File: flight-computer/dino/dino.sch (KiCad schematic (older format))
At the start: 5 parts

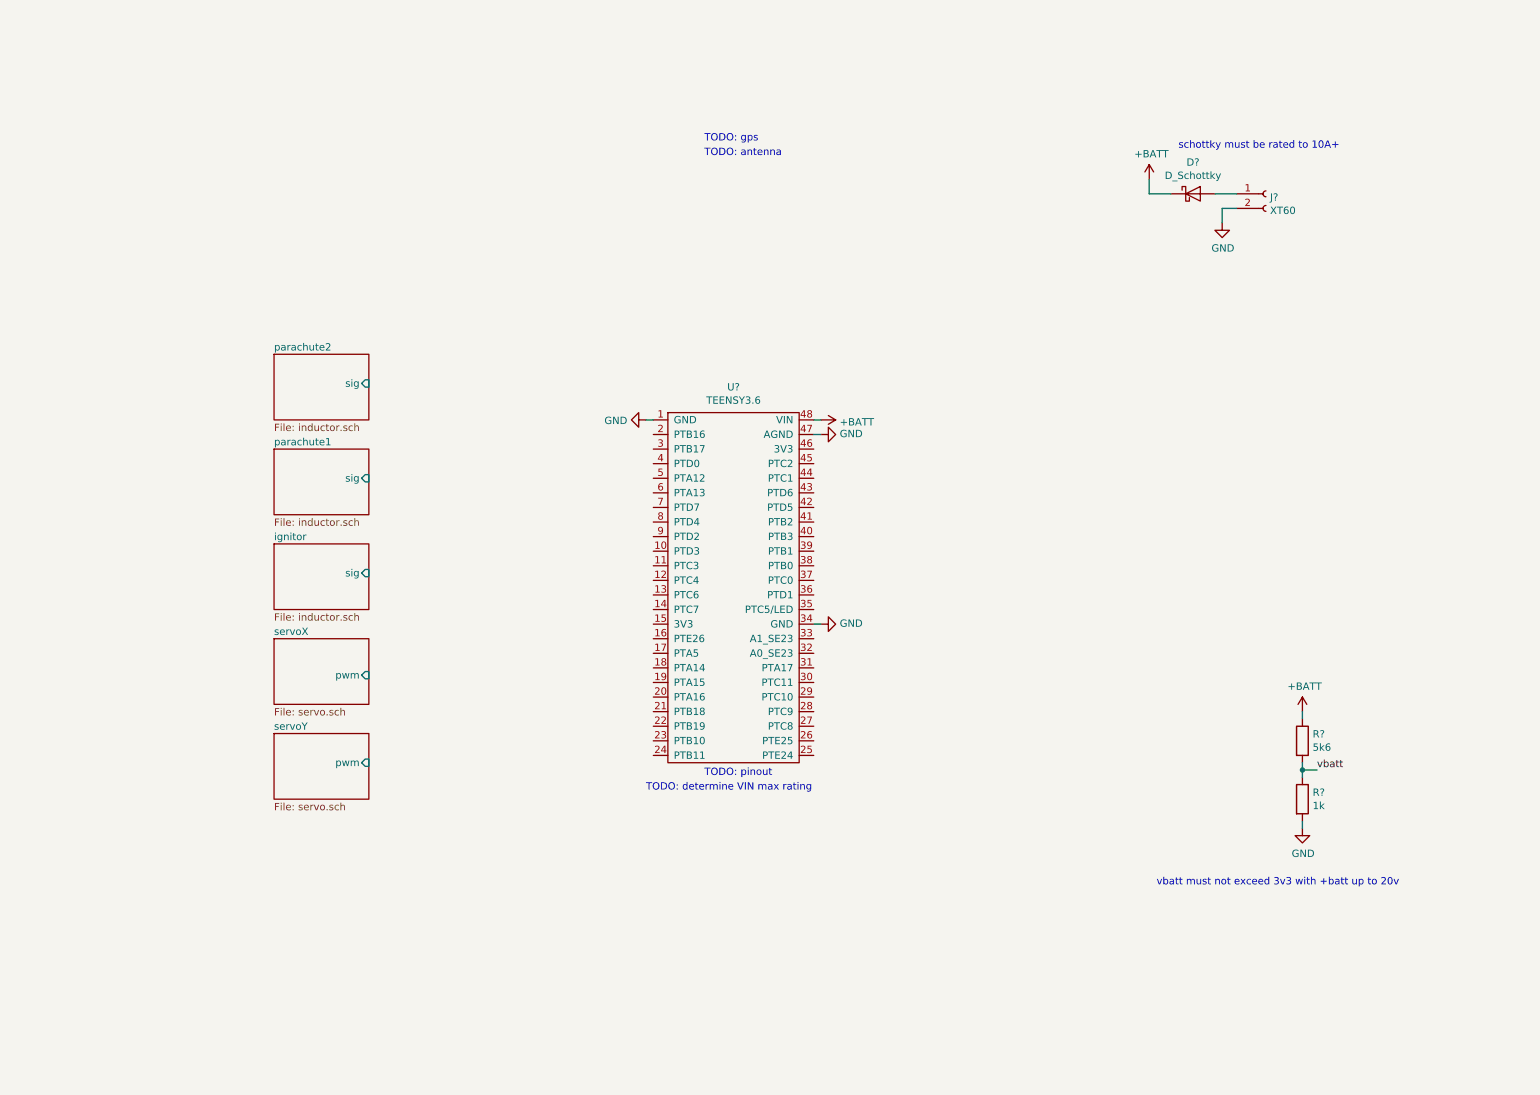
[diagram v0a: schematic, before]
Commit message: more pcb component selection
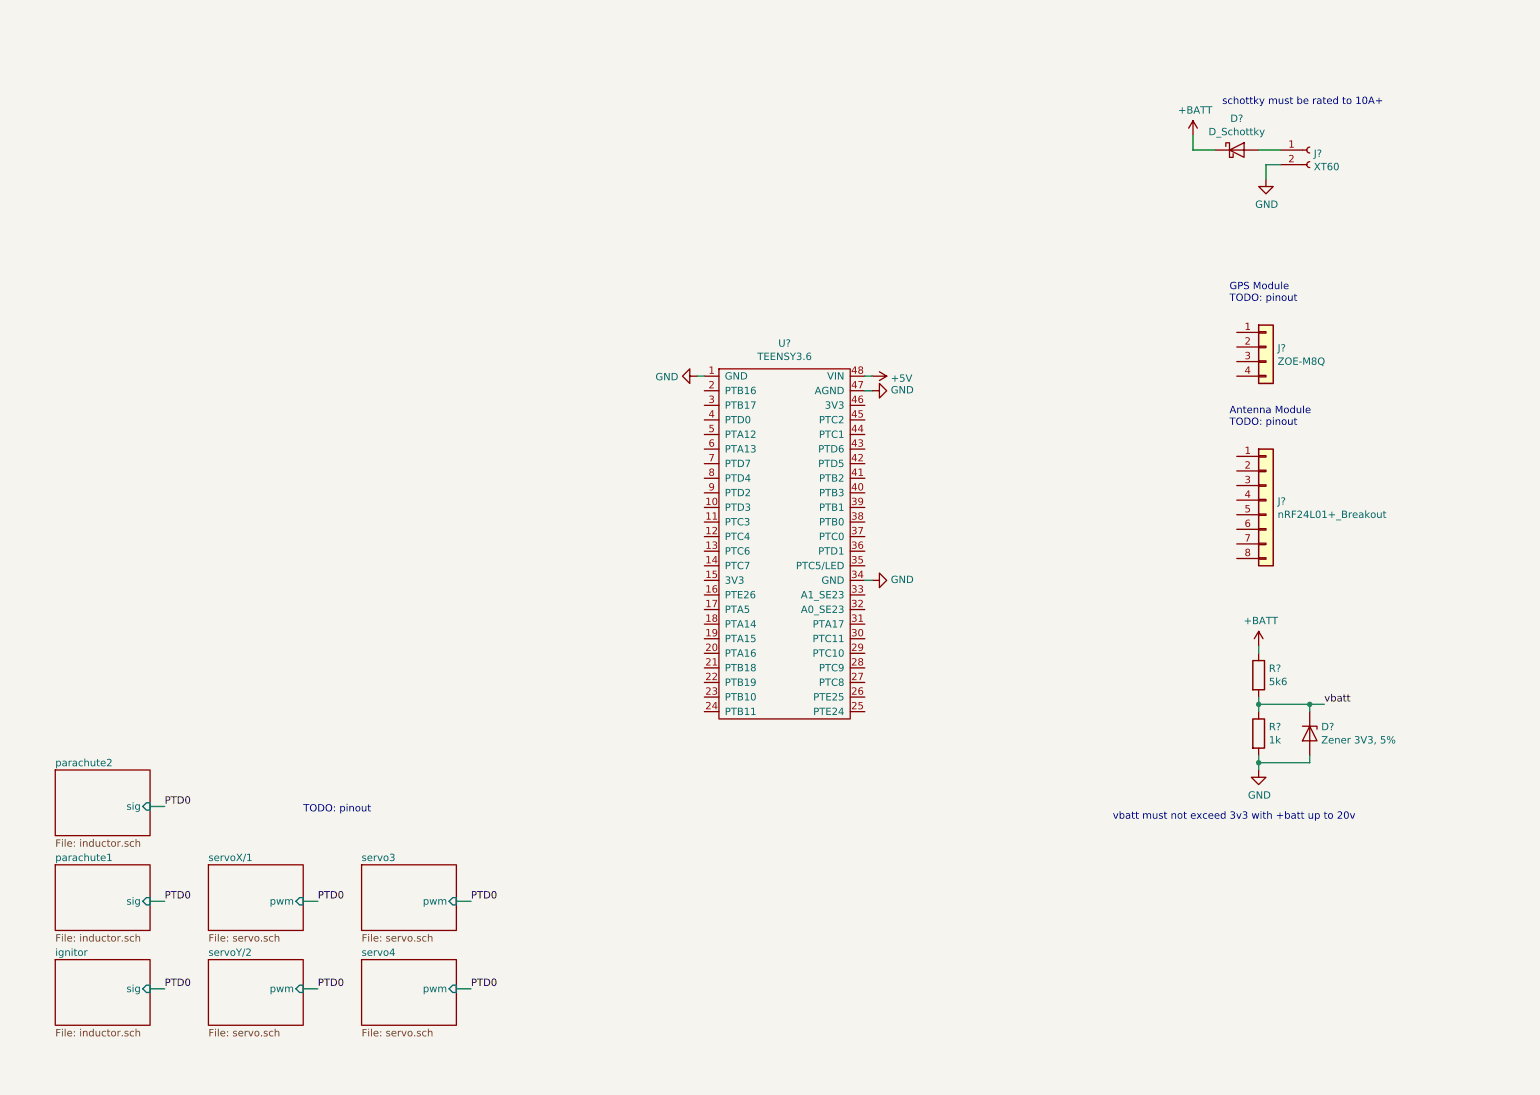
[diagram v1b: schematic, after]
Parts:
- added D?: Zener 3V3, 5%, symbol Device:D_Zener
- added J?: nRF24L01+_Breakout, symbol Connector_Generic:Conn_01x08
- added J?: ZOE-M8Q, symbol Connector_Generic:Conn_01x04
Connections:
- net +BATT: no longer U?.48 (VIN)
- net GND: now also D?.2 (A)
- net vbatt: now also D?.1 (K)
- new net +5V: U?.48 (VIN)
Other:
- note added: "Antenna Module\nTODO: pinout"
- note added: "GPS Module\nTODO: pinout"
- note removed: "TODO: antenna"
- note removed: "TODO: determine VIN max rating"
- note removed: "TODO: gps"
- moved on the sheet: D?, J?, R?, U?

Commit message: fc schematic fleshing-out and mcu docs
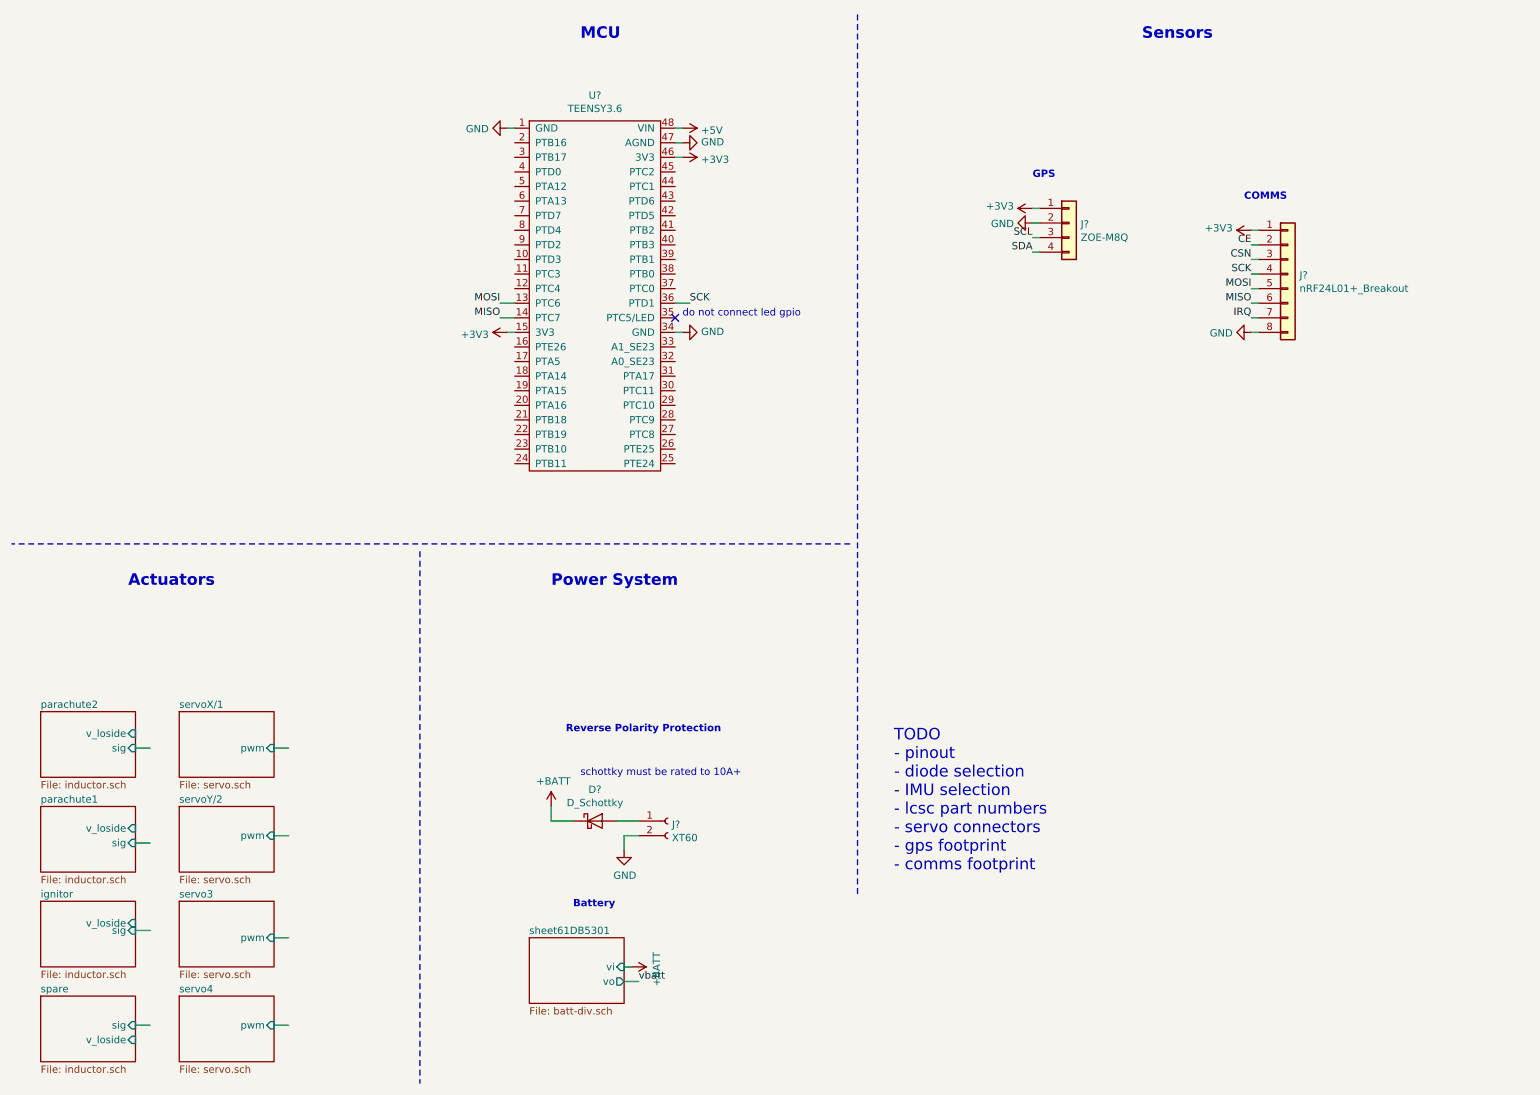
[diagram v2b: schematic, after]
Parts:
- removed D?: Zener 3V3, 5%, symbol Device:D_Zener
- removed R?: 5k6, symbol Device:R
- removed R?: 1k, symbol Device:R
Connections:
- net labels added: +3V3, CE, CSN, IRQ, MISO, MOSI, SCK, SCL, SDA
- net labels removed: PTD0
- wire segments 26 -> 36
- no-connect marks 0 -> 1
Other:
- note added: "Actuators"
- note added: "Battery"
- note added: "COMMS"
- note added: "GPS"
- note added: "MCU"
- note added: "Power System"
- note added: "Reverse Polarity Protection"
- note added: "Sensors"
- note added: "TODO\n- pinout\n- diode selection\n- IMU selection\n- lcsc part numbers\n- servo connectors\n- gps footprint\n- comms footprint"
- note added: "do not connect led gpio"
- note removed: "Antenna Module\nTODO: pinout"
- note removed: "GPS Module\nTODO: pinout"
- note removed: "TODO: pinout"
- note removed: "vbatt must not exceed 3v3 with +batt up to 20v"
- moved on the sheet: D?, J?, U?

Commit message: fc pinout and component selection. general cleanup
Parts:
- removed D?: D_Schottky, symbol Device:D_Schottky
- added C? (x3): 10u, Capacitor_Tantalum_SMD:CP_EIA-3216-18_Kemet-A, symbol Device:CP1_Small
- added D?: 40V 5A 550mV, Diode_SMD:D_SMA, symbol Device:D_Schottky
- added D? (x5): R, Diode_SMD:D_0603_1608Metric, symbol Device:LED_Small
- added D? (x7): W, Diode_SMD:D_0603_1608Metric, symbol Device:LED_Small
- added R? (x6): 10k, Resistor_SMD:R_0603_1608Metric, symbol Device:R_Small
- added R? (x6): 1k, Resistor_SMD:R_0603_1608Metric, symbol Device:R_Small
- added TP?: TestPoint, TestPoint:TestPoint_Keystone_5010-5014_Multipurpose, symbol Connector:TestPoint
- added U?: AMS1117-3.3, Package_TO_SOT_SMD:SOT-223-3_TabPin2, symbol Regulator_Linear:AMS1117-3.3
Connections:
- net labels added: fault, ign_sig, ign_vhi, ign_vlo, p1_sig, p1_vhi, p1_vlo, p2_sig, p2_vhi, p2_vlo, pwm_servo3, pwm_servo4, pwm_servoX, pwm_servoY, sp_sig, sp_vhi, sp_vlo, state_armed, state_burn, state_coast, state_init, state_recovery
- wire segments 36 -> 128
- no-connect marks 1 -> 2
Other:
- note added: "Arming"
- note added: "Battery Measurement"
- note added: "Indicators"
- note added: "LAYOUT: decoupling cap must be close to chip"
- note added: "LAYOUT: indicators must be clearly\nlabelled on silkscreen"
- note added: "Maintainer Notes\n- Designed for JLCPCB fab\n- Prefer JLCPCB "basic parts"\n- 2 layer board for cost"
- note added: "Power"
- note added: "State"
- note added: "TODO\n- comms pinout/connections\n- IMU selection\n- servo connectors\n- gps footprint\n- comms footprint"
- note added: "Voltage Regulation"
- note added: "adc inputs"
- note added: "armed indicators must\nbe hardware controlled"
- note added: "gpio"
- note added: "i2c 2"
- note added: "schottky must be rated to 5A+"
- note added: "servos on FTM3, CH4-7"
- note added: "spi 0"
- note removed: "Battery"
- note removed: "TODO\n- pinout\n- diode selection\n- IMU selection\n- lcsc part numbers\n- servo connectors\n- gps footprint\n- comms footprint"
- note removed: "schottky must be rated to 10A+"
- moved on the sheet: J?, U?
